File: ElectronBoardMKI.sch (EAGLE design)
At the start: 22 parts

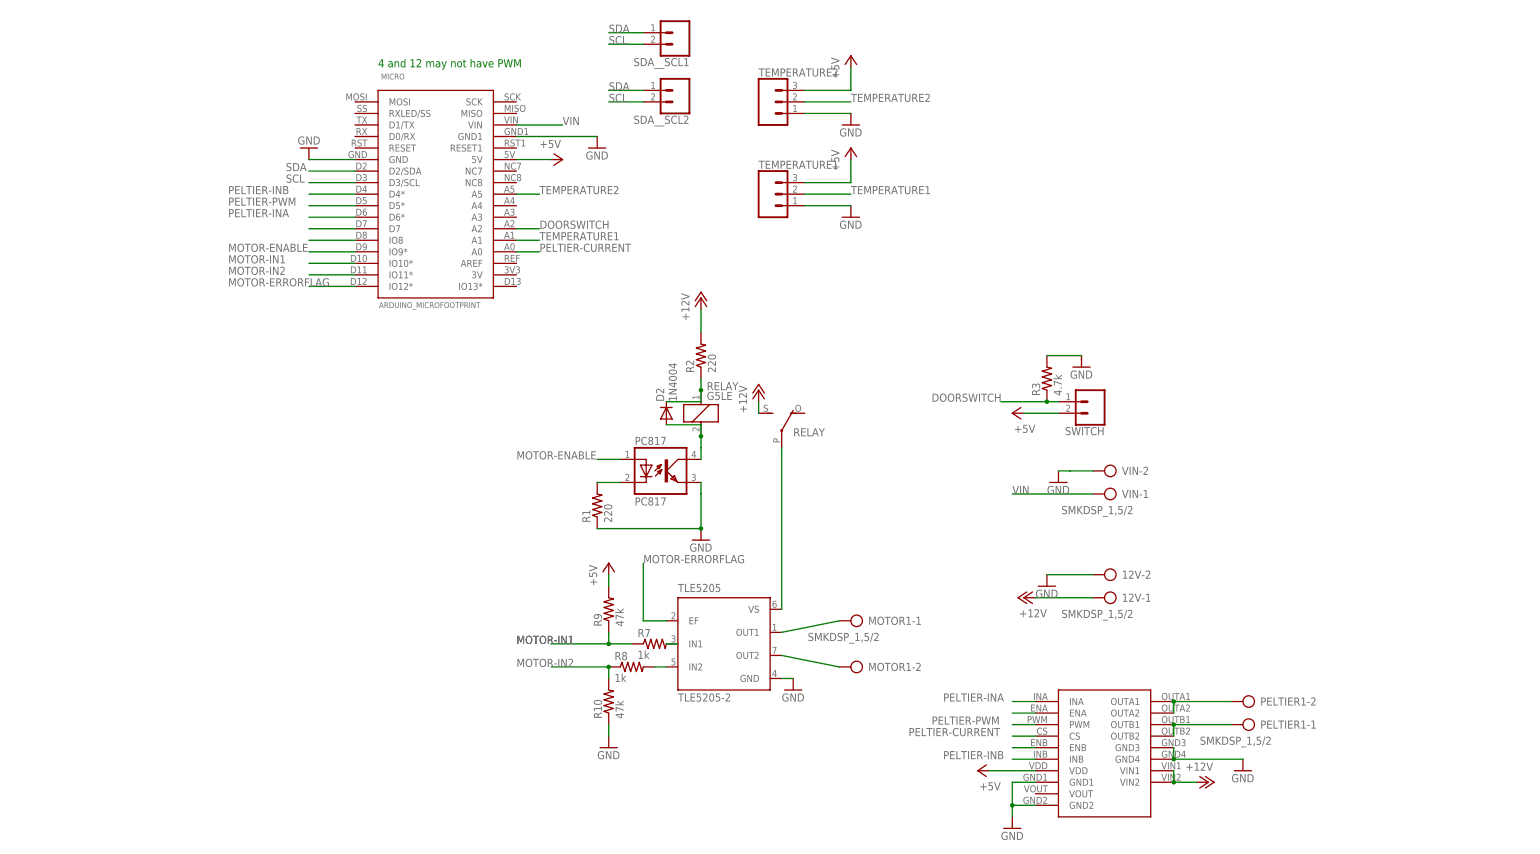
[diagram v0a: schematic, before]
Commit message: Updated PCB VIAS +more
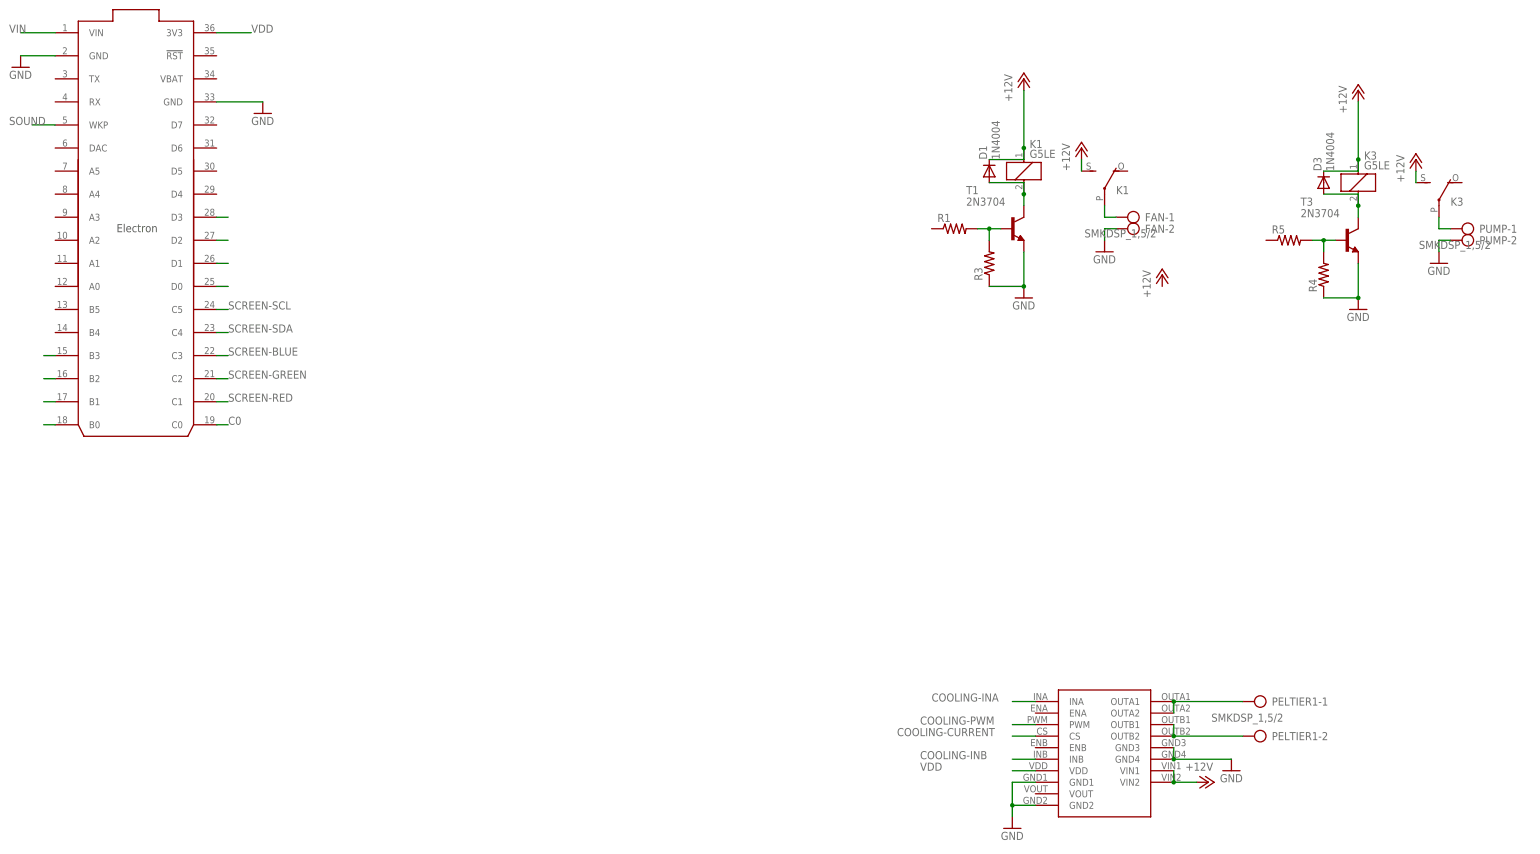
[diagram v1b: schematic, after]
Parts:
- removed 12V, MOTOR1, VIN: SMKDSP_1,5/2, con-phoenix-smkdsp:SMKDSP_1,5/2
- removed D2: 1N4004, diode:1N4004
- removed MICRO: ARDUINO_MICROFOOTPRINT, arduino-micro:ARDUINO_MICROFOOTPRINT
- removed PC817: PC817, optocoupler:PC817
- removed R10, R9: 47k, resistor:R-US_0207/12
- removed R2: 220, resistor:R-US_0207/12
- removed R7, R8: 1k, resistor:R-US_0207/12
- removed RELAY: G5LE, relay:G5LE
- removed SDA__SCL1, SDA__SCL2, SWITCH: (no value), SparkFun-Connectors:CONN_02PTH3
- removed TEMPERATURE1, TEMPERATURE2: (no value), SparkFun-Connectors:CONN_03LONGPADS
- removed TLE5205: TLE5205-2, infineon:TLE5205-2
- added D1, D3: 1N4004, diode:1N4004
- added FAN, PUMP: SMKDSP_1,5/2, con-phoenix-smkdsp:SMKDSP_1,5/2
- added K1, K3: G5LE, relay:G5LE
- added R4, R5: (no value), resistor:R-US_0207/12
- added T1, T3: 2N3704, transistor:2N3704
- added U$1: ELECTRON_WITH_HEADERS, Particle-Devices:ELECTRON_WITH_HEADERS
- R1: value 220 -> (none)
- R3: value 4.7k -> (none)
- renumbered VNH5019 to U$2
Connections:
- removed net +5V: MICRO.5V, R9.2, SWITCH.2, TEMPERATURE1.3, TEMPERATURE2.3, U$2.VDD
- removed net DOORSWITCH: MICRO.A2, R3.1, SWITCH.1
- removed net MOTOR-ENABLE: MICRO.IO9*, PC817.A
- removed net MOTOR-ERRORFLAG: MICRO.IO12*, TLE5205.EF
- removed net MOTOR-IN1: MICRO.IO10*, R7.1, R9.1
- removed net MOTOR-IN2: MICRO.IO11*, R10.2, R8.1
- removed net N$10: R7.2, TLE5205.IN1
- removed net N$13: R8.2, TLE5205.IN2
- removed net N$14: U$2.ENA
- removed net N$18: U$2.ENB
- removed net N$21: MICRO.D7
- removed net N$22: MICRO.IO8
- removed net N$3: D2.A, PC817.COL, RELAY1.2
- removed net N$4: RELAY2.P, TLE5205.VS
- removed net N$6: MOTOR1-1.KL, TLE5205.OUT1
- removed net N$7: MOTOR1-2.KL, TLE5205.OUT2
- removed net PELTIER-CURRENT: MICRO.A0, U$2.CS
- removed net PELTIER-INA: MICRO.D6*, U$2.INA
- removed net PELTIER-INB: MICRO.D4*, U$2.INB
- removed net PELTIER-PWM: MICRO.D5*, U$2.PWM
- removed net SCL: MICRO.D3/SCL, SDA__SCL1.2, SDA__SCL2.2
- removed net SDA: MICRO.D2/SDA, SDA__SCL1.1, SDA__SCL2.1
- removed net TEMPERATURE1: MICRO.A1, TEMPERATURE1.2
- removed net TEMPERATURE2: MICRO.A5, TEMPERATURE2.2
- new net C0: U$1.C0
- new net COOLING-CURRENT: U$2.CS
- new net COOLING-INA: U$2.INA
- new net COOLING-INB: U$2.INB
- new net COOLING-PWM: U$2.PWM
- new net N$11: K32.P, PUMP-1.KL
- new net N$12: R4.2, R5.2, T3.B
- new net N$2: D1.A, K11.2, T1.C
- new net N$23: U$1.D0
- new net N$24: U$1.D1
- new net N$25: U$1.D2
- new net N$26: U$1.D3
- new net N$27: U$1.B0
- new net N$28: U$1.B1
- new net N$29: U$1.B2
- new net N$30: U$1.B3
- new net N$9: D3.A, K31.2, T3.C
- new net SCREEN-BLUE: U$1.C3
- new net SCREEN-GREEN: U$1.C2
- new net SCREEN-RED: U$1.C1
- new net SCREEN-SCL: U$1.C5
- new net SCREEN-SDA: U$1.C4
- new net SOUND: U$1.WKP
- new net VDD: U$1.3V3, U$2.VDD
- net +12V: now also D1.C, D3.C, K11.1, K12.S, K31.1, K32.S; no longer 12V-1.KL, R2.2, RELAY2.S
- net GND: now also FAN-2.KL, PUMP-2.KL, R3.1, R4.1, T1.E, T3.E, U$1.GND@2, U$1.GND@21; no longer 12V-2.KL, MICRO.GND, MICRO.GND1, PC817.EMIT, R1.1, R10.1, R3.2, TEMPERATURE1.1, TEMPERATURE2.1, TLE5205.GND, VIN-2.KL
- net N$1: now also R3.2, T1.B; no longer PC817.C
- net N$16: now also PELTIER1-2.KL; no longer PELTIER1-1.KL
- net N$17: now also PELTIER1-1.KL; no longer PELTIER1-2.KL
- net N$5: now also FAN-1.KL, K12.P; no longer D2.C, R2.1, RELAY1.1
- net VIN: now also U$1.VIN; no longer MICRO.VIN, VIN-1.KL
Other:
- note removed: "4 and 12 may not have PWM"
- moved on the sheet: PELTIER1-1, PELTIER1-2, R1, R3

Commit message: ElectornBoard PCB
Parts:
- removed D1, D3: 1N4004, diode:1N4004
- removed K1, K3: G5LE, relay:G5LE
- removed PELTIER1: SMKDSP_1,5/2, con-phoenix-smkdsp:SMKDSP_1,5/2
- removed T1: 2N3704, transistor:2N3704
- added 12V, SPEAKER, VIN: SMKDSP_1,5/2, con-phoenix-smkdsp:SMKDSP_1,5/2
- added C1: 10uf, resistor:CPOL-USE5-8.5
- added C2: 1uf, resistor:CPOL-USE5-8.5
- added IC1: 7805TV, linear:7805TV
- added IN-TEMP, OUT-TEMP: (no value), SparkFun-Connectors:CONN_03LOCK_LONGPADS
- added J1: (no value), SparkFun-Connectors:CONN_08LOCK_LONGPADS
- added Q1, Q2: TN0602N3, transistor-fet:TN0602N3
- added R10, R7: 47k, resistor:R-US_0207/12
- added R11, R6, R8: 36, resistor:R-US_0207/12
- added R12, R13, R14, R15: 4.7k, resistor:R-US_0207/12
- added R2, R9: 1k, resistor:R-US_0207/12
- added SCL__SDA1, SCL__SDA2: (no value), SparkFun-Connectors:CONN_02LOCK_LONGPADS
- added SCREEN: (no value), SparkFun-Connectors:CONN_05X2SHD
- added T2, T4: 2N2222, transistor:2N2222
- R1, R3: value (none) -> 4.7k
- R4: value (none) -> 1k
- R5: value (none) -> 47k
- T3: value 2N3704 -> 2N2222; device transistor:2N3704 -> transistor:2N2222
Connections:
- removed net C0: U$1.C0
- removed net N$1: R1.2, R3.2, T1.B
- removed net N$17: PELTIER1-1.KL, U$2.OUTA1, U$2.OUTA2
- removed net N$2: D1.A, K11.2, T1.C
- removed net N$23: U$1.D0
- removed net N$24: U$1.D1
- removed net N$25: U$1.D2
- removed net N$26: U$1.D3
- removed net N$27: U$1.B0
- removed net N$28: U$1.B1
- removed net N$29: U$1.B2
- removed net N$30: U$1.B3
- removed net N$5: FAN-1.KL, K12.P
- removed net VDD: U$1.3V3, U$2.VDD
- new net 3V3: IN-TEMP.3, OUT-TEMP.3, Q1.G, Q2.G, R1.2, R12.2, R14.2, R3.2, SCREEN.6, U$1.3V3, U$2.VDD
- new net 5V: C2.+, IC1.VO, R13.2, R15.2
- new net IN-TEMP: IN-TEMP.2, U$1.DAC
- new net KEYPAD-1: J1.3, U$1.B4
- new net KEYPAD-2: J1.4, U$1.B3
- new net KEYPAD-3: J1.5, U$1.B2
- new net KEYPAD-A: J1.1, U$1.A0
- new net KEYPAD-B: J1.2, U$1.B5
- new net KEYPAD-C: J1.8, U$1.B0
- new net KEYPAD-D: J1.7, U$1.B1
- new net N$10: FAN-1.KL, PUMP-1.KL, U$2.OUTB1, U$2.OUTB2
- new net N$13: R4.2, R7.2, T3.B
- new net N$14: R8.2, T3.E
- new net N$15: R10.2, R9.2, T4.B
- new net N$3: U$1.A4
- new net N$8: U$1.D5
- new net OUT-TEMP: OUT-TEMP.2, U$1.A1
- new net SCL-3V3: Q1.S, R12.1, U$1.D1
- new net SCL-5V: Q1.D, R13.1, SCL__SDA1.2, SCL__SDA2.2
- new net SCREEN-BLUE-CONTROL: R2.1, U$1.C3
- new net SCREEN-GREEN-CONTROL: R9.1, U$1.C2
- new net SCREEN-RED-CONTROL: R4.1, U$1.C1
- new net SDA-3V3: Q2.S, R14.1, U$1.D0
- new net SDA-5V: Q2.D, R15.1, SCL__SDA1.1, SCL__SDA2.1
- net +12V: now also 12V-1.KL; no longer D1.C, D3.C, K11.1, K12.S, K31.1, K32.S
- net COOLING-CURRENT: now also U$1.A3
- net COOLING-INA: now also U$1.D2
- net COOLING-INB: now also U$1.D4
- net COOLING-PWM: now also U$1.D3
- net GND: now also 12V-2.KL, C1.-, C2.-, IC1.GND, IN-TEMP.1, OUT-TEMP.1, R10.1, R11.1, R5.1, R6.1, R7.1, R8.1, SCREEN.10, SCREEN.3, SCREEN.4, SCREEN.8, SPEAKER-2.KL, VIN-2.KL; no longer FAN-2.KL, PUMP-2.KL, R3.1, R4.1, T1.E, T3.E
- net N$11: now also R2.2, R5.2, T2.B; no longer K32.P, PUMP-1.KL
- net N$12: now also R6.2, T2.E; no longer R4.2, R5.2, T3.B
- net N$16: now also R11.2, T4.E; no longer PELTIER1-2.KL, U$2.OUTB1, U$2.OUTB2
- net N$9: now also FAN-2.KL, PUMP-2.KL, U$2.OUTA1, U$2.OUTA2; no longer D3.A, K31.2, T3.C
- net SCREEN-BLUE: now also SCREEN.5, T2.C; no longer U$1.C3
- net SCREEN-GREEN: now also SCREEN.7, T4.C; no longer U$1.C2
- net SCREEN-RED: now also SCREEN.9, T3.C; no longer U$1.C1
- net SCREEN-SCL: now also R1.1, SCREEN.1
- net SCREEN-SDA: now also R3.1, SCREEN.2
- net SOUND: now also SPEAKER-1.KL
- net VIN: now also C1.+, IC1.VI, VIN-1.KL
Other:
- moved on the sheet: FAN-1, FAN-2, PUMP-1, PUMP-2, R1, R3, R4, R5, T3

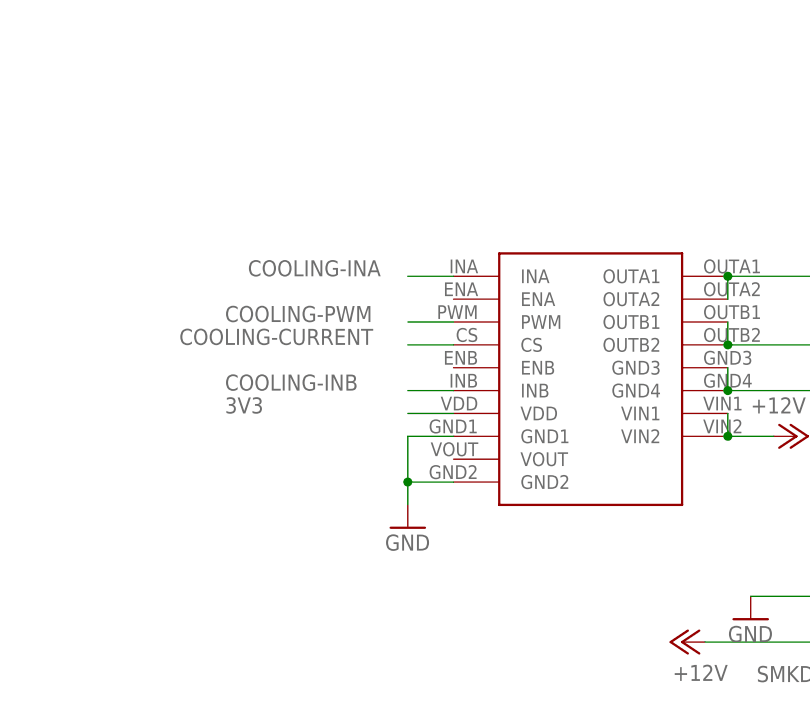
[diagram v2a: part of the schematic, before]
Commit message: Net Lables + Pull-Down Resistors on Electron
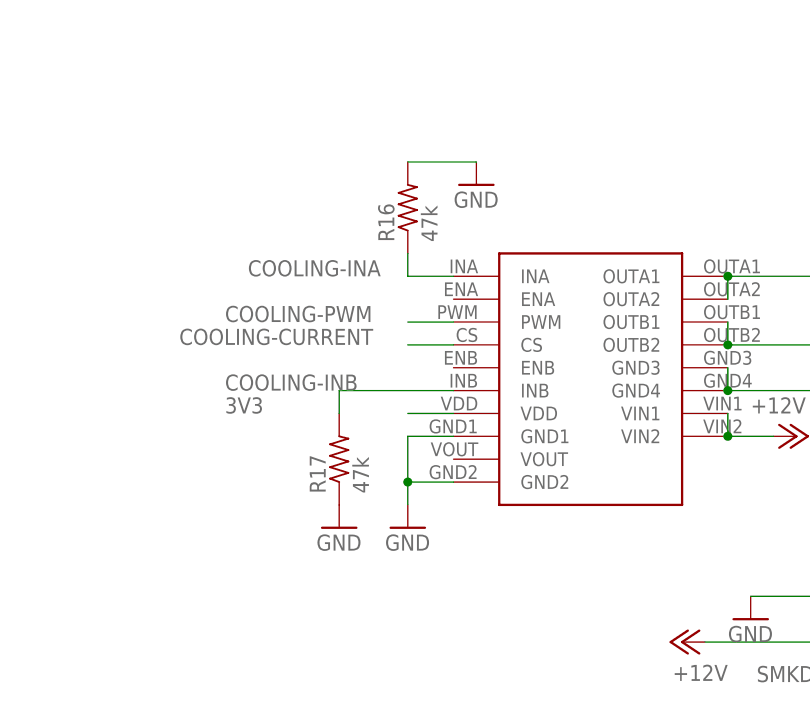
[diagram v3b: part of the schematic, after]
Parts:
- added R16, R17: 47k, resistor:R-US_0207/12
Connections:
- net N$10 renamed COOLING-OUTB
- net N$11 renamed BLUE-NPN-BASE
- net N$12 renamed BLUE-NPN-EMITTER
- net N$13 renamed RED-NPN-BASE
- net N$14 renamed RED-NPN-EMITTER
- net N$15 renamed GREEN-NPN-BASE
- net N$16 renamed GREEN-NPN-EMITTER
- net N$9 renamed COOLING-OUTA
- net COOLING-INA: now also R16.1
- net COOLING-INB: now also R17.2
- net GND: now also R16.2, R17.1
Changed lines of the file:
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@@
 <part name="R1" library="resistor" library_urn="urn:adsk.eagle:library:348" deviceset="R-US_" device="0207/12" package3d_urn="urn:adsk.eagle:package:25938/1" value="4.7k"/>
 <part name="R3" library="resistor" library_urn="urn:adsk.eagle:library:348" deviceset="R-US_" device="0207/12" package3d_urn="urn:adsk.eagle:package:25938/1" value="4.7k"/>
+<part name="R16" library="resistor" library_urn="urn:adsk.eagle:library:348" deviceset="R-US_" device="0207/12" package3d_urn="urn:adsk.eagle:package:25938/1" value="47k"/>
+<part name="R17" library="resistor" library_urn="urn:adsk.eagle:library:348" deviceset="R-US_" device="0207/12" package3d_urn="urn:adsk.eagle:package:25938/1" value="47k"/>
+<part name="GND2" library="supply1" library_urn="urn:adsk.eagle:library:371" deviceset="GND" device=""/>
+<part name="GND3" library="supply1" library_urn="urn:adsk.eagle:library:371" deviceset="GND" device=""/>
 </parts>
 <sheets>
@@
 <instance part="R1" gate="G$1" x="-25.4" y="68.58" rot="R90"/>
 <instance part="R3" gate="G$1" x="-5.08" y="68.58" rot="R90"/>
+<instance part="R16" gate="G$1" x="-139.7" y="-22.86" rot="R90"/>
+<instance part="R17" gate="G$1" x="-147.32" y="-50.8" rot="R90"/>
+<instance part="GND2" gate="1" x="-147.32" y="-58.42"/>
+<instance part="GND3" gate="1" x="-132.08" y="-20.32"/>
 </instances>
 <busses>
@@
 <wire x1="109.22" y1="104.14" x2="109.22" y2="106.68" width="0.1524" layer="91"/>
 </segment>
+<segment>
+<pinref part="R17" gate="G$1" pin="1"/>
+<pinref part="GND2" gate="1" pin="GND"/>
+</segment>
+<segment>
+<pinref part="R16" gate="G$1" pin="2"/>
+<pinref part="GND3" gate="1" pin="GND"/>
+<wire x1="-139.7" y1="-17.78" x2="-132.08" y2="-17.78" width="0.1524" layer="91"/>
+</segment>
 </net>
 <net name="+12V" class="0">
@@
 <wire x1="-134.62" y1="-30.48" x2="-139.7" y2="-30.48" width="0.1524" layer="91"/>
 <label x="-157.48" y="-30.48" size="1.778" layer="95"/>
+<pinref part="R16" gate="G$1" pin="1"/>
+<wire x1="-139.7" y1="-27.94" x2="-139.7" y2="-30.48" width="0.1524" layer="91"/>
 </segment>
 <segment>
@@
 <segment>
 <pinref part="U$2" gate="G$1" pin="INB"/>
-<wire x1="-134.62" y1="-43.18" x2="-139.7" y2="-43.18" width="0.1524" layer="91"/>
 <label x="-160.02" y="-43.18" size="1.778" layer="95"/>
+<pinref part="R17" gate="G$1" pin="2"/>
+<wire x1="-147.32" y1="-45.72" x2="-147.32" y2="-43.18" width="0.1524" layer="91"/>
+<wire x1="-147.32" y1="-43.18" x2="-134.62" y2="-43.18" width="0.1524" layer="91"/>
 </segment>
 <segment>
@@
 </segment>
 </net>
-<net name="N$9" class="0">
+<net name="COOLING-OUTA" class="0">
 <segment>
 <pinref part="U$2" gate="G$1" pin="OUTA1"/>
@@
 </segment>
 </net>
-<net name="N$10" class="0">
+<net name="COOLING-OUTB" class="0">
 <segment>
 <pinref part="U$2" gate="G$1" pin="OUTB1"/>
@@
 </segment>
 </net>
-<net name="N$11" class="0">
+<net name="BLUE-NPN-BASE" class="0">
 <segment>
 <pinref part="R2" gate="G$1" pin="2"/>
@@
 </segment>
 </net>
-<net name="N$12" class="0">
+<net name="BLUE-NPN-EMITTER" class="0">
 <segment>
 <pinref part="R6" gate="G$1" pin="2"/>
@@
 </segment>
 </net>
-<net name="N$13" class="0">
+<net name="RED-NPN-BASE" class="0">
 <segment>
 <pinref part="R4" gate="G$1" pin="2"/>
@@
 </segment>
 </net>
-<net name="N$14" class="0">
+<net name="RED-NPN-EMITTER" class="0">
 <segment>
 <pinref part="R8" gate="G$1" pin="2"/>
@@
 </segment>
 </net>
-<net name="N$15" class="0">
+<net name="GREEN-NPN-BASE" class="0">
 <segment>
 <pinref part="R9" gate="G$1" pin="2"/>
@@
 </segment>
 </net>
-<net name="N$16" class="0">
+<net name="GREEN-NPN-EMITTER" class="0">
 <segment>
 <pinref part="R11" gate="G$1" pin="2"/>

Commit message: Audio
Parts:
- added C3: 250uf, resistor:CPOL-USE5-8.5
- added C7: 10uf, resistor:CPOL-USE5-8.5
- added C8: 0.05uf, resistor:CPOL-USE5-8.5
- added C9: 1uf, resistor:CPOL-USE5-8.5
- added R19: 10k, resistor:R-US_0207/12
- added R21, R22: 10k, pot:TRIM_US-CT6
- added U1: LM386N, SparkFun-IC-Amplifiers:LM386
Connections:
- new net N$1: R21.S, U1.-IN
- new net N$2: C9.+, U1.BP
- new net N$4: R22.A, U1.GAIN@1
- new net N$5: C7.-, U1.GAIN@8
- new net N$6: C3.+, C8.+, U1.OUT
- new net N$7: C8.-, R19.2
- new net N$9: C7.+, R22.S
- new net SPEAKER-OUTPUT: C3.-, SPEAKER-1.KL
- net GND: now also C9.-, R19.1, R21.A, U1.+IN, U1.V-
- net SOUND: now also R21.E; no longer SPEAKER-1.KL
- net VIN: now also U1.V+
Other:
- note added: "4V-12V"
- note added: "Audio Power Amplifier with Controlled Gain"
- note added: "By varying R3 across pin 1 and 8, Gain can be varied from 20 to 200"
- note added: "Example, if Gain is 20, then volume range is 0 to 20"
- note added: "Gain = 20 - 200"
- note added: "Gain = 30000/(150+R3)"
- note added: "Gain sets the range of possible volume levels"
- note added: "If gain is 200 then range volume range extends from 0 to 200"
- note added: "Potentiometer R1 act as volume control knob"
- note added: "R2 and C2 act as filter to remove sudden High frequency oscillations"
- note added: "R3 = 150+(30000/Gain)"
- note added: "Useful Notes"
